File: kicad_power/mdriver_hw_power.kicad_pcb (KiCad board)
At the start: 4 copper layers, 115.4 x 107.7 mm, 69 parts, among them J1 Conn_02x05_Odd_Even, J2 Conn_01x02, M1 Fan, Q1 NMOS, Q2 NMOS, Q3 NMOS, Q4 NMOS, Q5 2N7002E, U7 SFH617A-1X007T

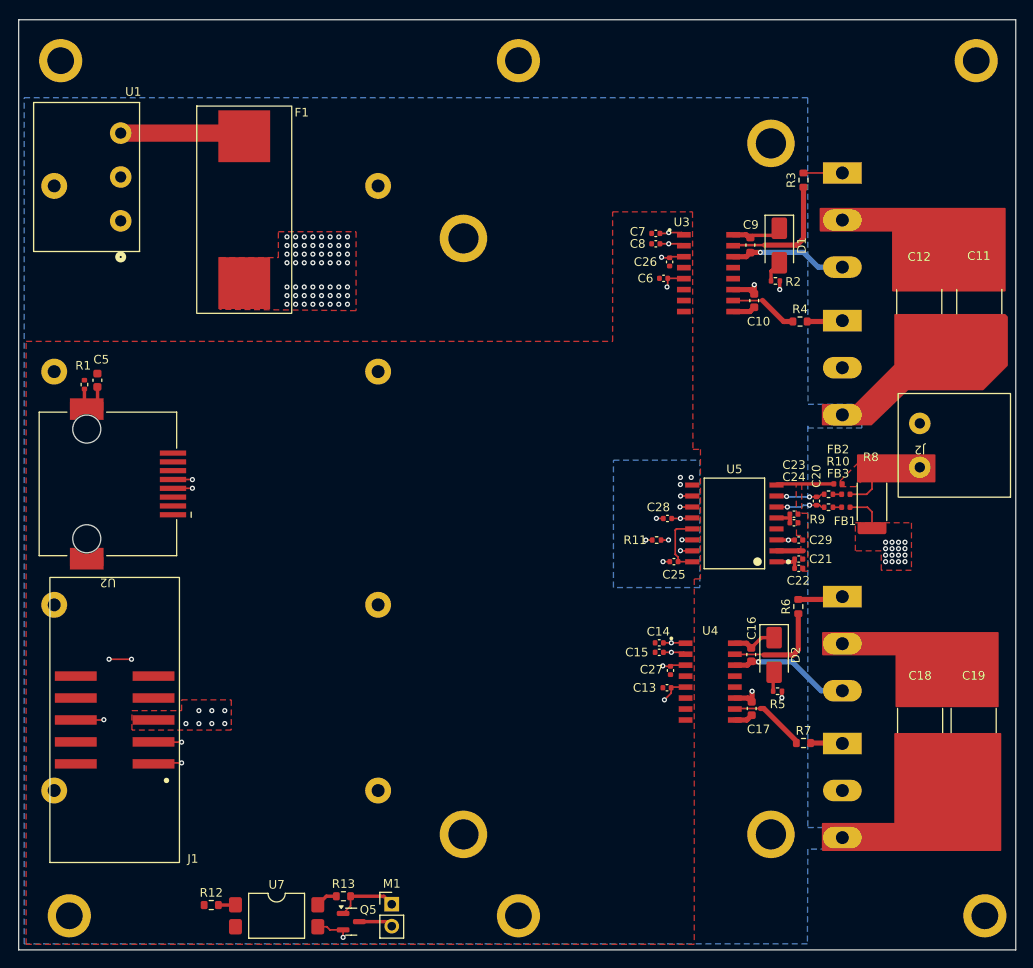
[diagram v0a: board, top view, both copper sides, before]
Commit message: adjustment to PCB layout, created BOM file, added MOSFET gate discharge diodes
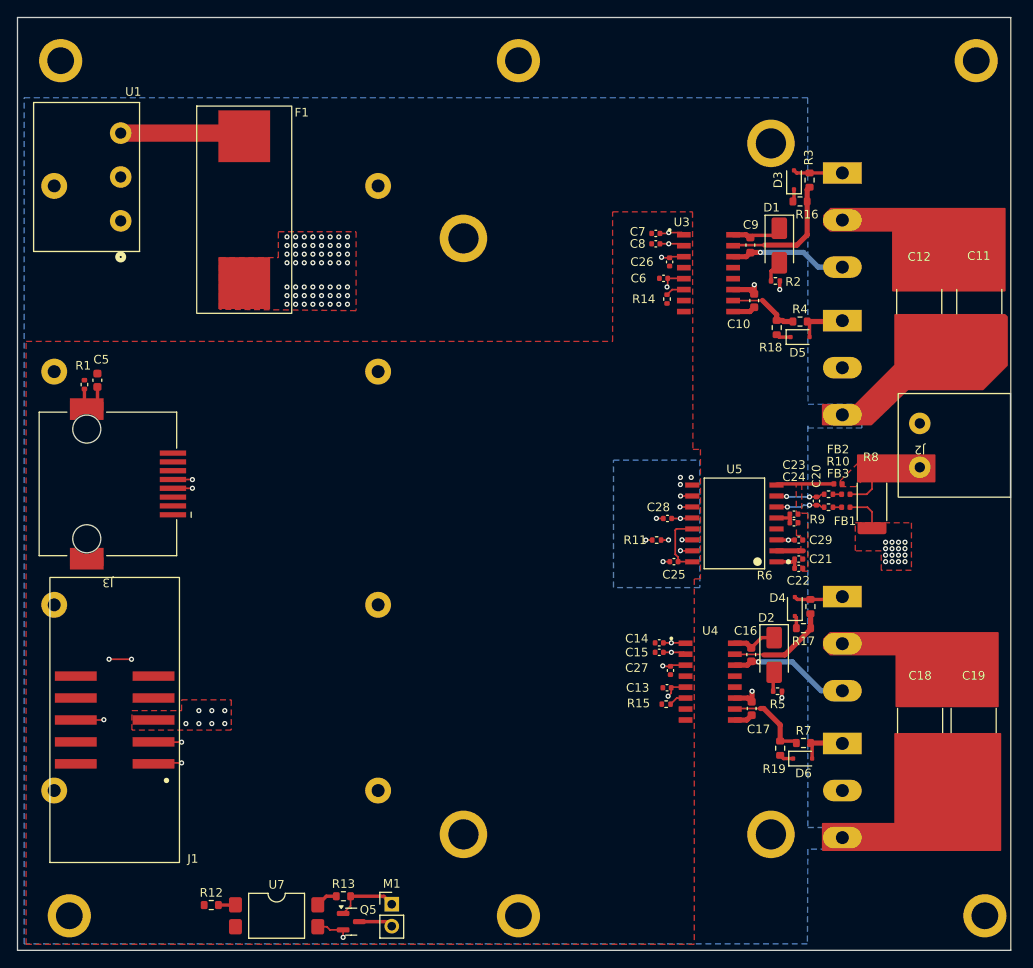
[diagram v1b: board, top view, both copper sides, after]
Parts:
- added D3: D_Schottky, Diode_SMD:D_SOD-323F, F.Cu at (153.9, 58.8)
- added D4: D_Schottky, Diode_SMD:D_SOD-323F, F.Cu at (154.0, 108.2)
- added D5: D_Schottky, Diode_SMD:D_SOD-323F, F.Cu at (154.6, 77.0)
- added D6: D_Schottky, Diode_SMD:D_SOD-323F, F.Cu at (154.9, 125.8)
- added R14: 0, Resistor_SMD:R_0402_1005Metric, F.Cu at (139.2, 72.6)
- added R15: 0, Resistor_SMD:R_0402_1005Metric, F.Cu at (139.1, 119.5)
- added R16: 3.3, Resistor_SMD:R_0603_1608Metric, F.Cu at (154.6, 61.3)
- added R17: 3.3, Resistor_SMD:R_0603_1608Metric, F.Cu at (155.0, 110.7)
- added R18: 3.3, Resistor_SMD:R_0603_1608Metric, F.Cu at (151.9, 75.9)
- added R19: 3.3, Resistor_SMD:R_0603_1608Metric, F.Cu at (152.3, 124.6)
- moved R6 1.40 mm to (155.8, 108.2)
- moved R3 0.70 mm to (155.7, 58.8)
- renumbered U2 to J3
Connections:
- U3 pad 6: ISOGND -> Net-(U3-DTC)
- U4 pad 6: ISOGND -> Net-(U4-DTC)
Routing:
- net Net-(U3-DTC): track 0.00 -> 2.19 mm
- net Net-(U4-DTC): track 0.00 -> 2.03 mm
- net Net-(D5-A): track 4.12 -> 6.03 mm
- net Net-(D6-A): track 3.70 -> 5.57 mm
- net Net-(D5-K): track 0.00 -> 1.71 mm
- net Net-(D6-K): track 0.00 -> 1.66 mm
- net Net-(D3-A): track 4.75 -> 6.26 mm
- net Net-(D4-K): track 0.00 -> 1.47 mm
- net Net-(D3-K): track 0.00 -> 1.45 mm
- net Net-(U4-OUTB): track 8.94 -> 10.1 mm
- net Net-(D4-A): track 5.23 -> 5.75 mm
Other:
- board size 115.4 x 107.7 mm -> 115 x 108 mm

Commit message: introduced AGND and A3V3, ensures HV design rules
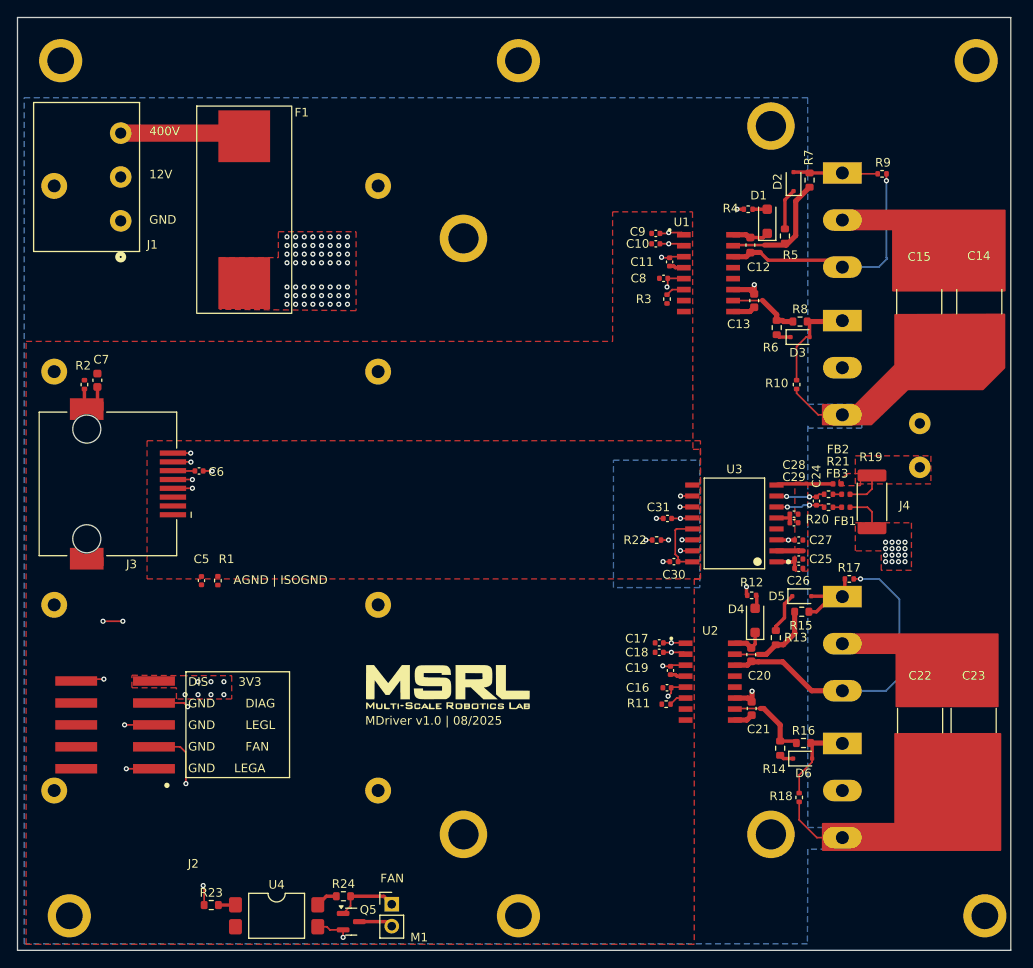
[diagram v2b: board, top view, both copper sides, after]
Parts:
- added C5: C, Capacitor_SMD:C_0402_1005Metric, F.Cu at (85.3, 105.2)
- added C6: 100nF, Capacitor_SMD:C_0402_1005Metric, F.Cu at (85.0, 92.5)
- added G***: LOGO, mdriver:msrl_logo, F.Cu at (114.2, 117.0)
- added R1: R, Resistor_SMD:R_0402_1005Metric, F.Cu at (87.2, 105.2)
- added R10: 560k, Resistor_SMD:R_0402_1005Metric, F.Cu at (154.2, 82.5)
- added R17: 560k, Resistor_SMD:R_0402_1005Metric, F.Cu at (160.3, 105.0)
- added R18: 560k, Resistor_SMD:R_0402_1005Metric, F.Cu at (154.5, 130.3)
- added R9: 560k, Resistor_SMD:R_0402_1005Metric, F.Cu at (164.1, 58.1)
- C12: renamed from C9; value 1uF -> 2.2u
- C13: renamed from C10; value 1uF -> 2.2u
- C20: renamed from C16; value 1uF -> 2.2u
- C21: renamed from C17; value 1uF -> 2.2u
- D1: footprint Diode_SMD:D_SMA -> Diode_SMD:D_SOD-123F
- D4: renamed from D2; footprint Diode_SMD:D_SMA -> Diode_SMD:D_SOD-123F
- R19: renamed from R8; value 3m -> 5m
- moved R12 11.5 mm to (149.0, 106.9), turned to 0 degrees
- moved R4 8.88 mm to (148.6, 62.2), turned to 0 degrees
- moved D4 4.57 mm to (149.4, 109.8), turned to 90 degrees
- moved R5 4.37 mm to (152.8, 65.3), turned to 90 degrees
- moved R13 3.38 mm to (151.8, 111.8), turned to 90 degrees
- moved D1 3.13 mm to (150.8, 63.6), turned to 90 degrees
- moved D5 1.44 mm to (154.8, 107.0), turned to 0 degrees
- moved R15 1.17 mm to (154.8, 108.8), turned to 0 degrees
- moved J2 0.57 mm to (75.3, 121.9)
- moved D2 0.21 mm to (153.8, 59.0)
- moved FB3 0.10 mm to (158.9, 94.0)
- renumbered C8 to C10, C26 to C11, C11 to C14, C12 to C15, C13 to C16, C14 to C17, C15 to C18, C27 to C19, C18 to C22, C19 to C23, C20 to C24, C21 to C25, C22 to C26, C29 to C27, C23 to C28, C24 to C29, C25 to C30, C28 to C31, C5 to C7, C6 to C8, C7 to C9, D3 to D2, D5 to D3, D4 to D5, U1 to J1, J1 to J2, J2 to J4, R15 to R11, R5 to R12, R17 to R13, R19 to R14, R6 to R15, R7 to R16, R1 to R2, R9 to R20, R10 to R21, R11 to R22, R12 to R23, R13 to R24, R14 to R3, R2 to R4, R16 to R5, R18 to R6, R3 to R7, R4 to R8, U3 to U1, U4 to U2, U5 to U3, U7 to U4
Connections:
- C30 pad 2: ISOGND -> AGND
- C31 pad 1: 3V3 -> A3V3
- C31 pad 2: ISOGND -> AGND
- J2 pad 2: ISOGND -> FAN
- J2 pad 4: ISOGND -> DIAG
- J3 pad 1: unconnected-(J3-Pad1) -> AGND
- J3 pad 2: unconnected-(J3-Pad2) -> AGND
- J3 pad 3: unconnected-(J3-Pad3) -> AGND
- J3 pad 6: unconnected-(J3-Pad6) -> /3V0ref
- J3 pad 7: unconnected-(J3-Pad7) -> A3V3
- J3 pad 8: unconnected-(J3-Pad8) -> A3V3
- R22 pad 1: 3V3 -> A3V3
- R22 pad 2: /isense/diag -> DIAG
- R23 pad 1: /fan/fan -> FAN
- U3 pad 12: 3V3 -> A3V3
- U3 pad 14: /isense/diag -> DIAG
- U3 pad 15: ISOGND -> AGND
- U3 pad 9: ISOGND -> AGND
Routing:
- net DIAG: track 0.00 -> 71.4 mm, vias 0 -> 3
- net /isense/in+: track 18.7 -> 41.3 mm
- net FAN: track 0.00 -> 22.5 mm, vias 0 -> 2
- net /legA/OUT: track 13.9 -> 29.4 mm
- net GND: track 3.95 -> 18.7 mm
- net A3V3: track 0.00 -> 7.31 mm, vias 0 -> 4
- net Net-(D5-A): track 5.75 -> 12.7 mm
- net DIS: track 200.1 -> 193.7 mm
- net Net-(D3-A): track 6.03 -> 11.9 mm
- net Net-(D6-A): track 5.57 -> 10.2 mm
- net LEGAH: track 194.4 -> 198.9 mm
- net Net-(D2-A): track 6.26 -> 10.4 mm
- net AGND: track 0.00 -> 3.76 mm, vias 0 -> 4
- net /isense/diag: track 3.66 -> 0.00 mm, vias 2 -> 0
- net Net-(D2-K): track 1.45 -> 4.79 mm
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- added copper zone on In1.Cu, net A3V3
- added copper zone on B.Cu, net AGND
- added copper zone on F.Cu, net AGND
- removed copper zone on B.Cu, net ISOGND
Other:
- board text added: "12V"
- board text added: "400V"
- board text added: "AGND | ISOGND"
- board text added: "DIS 3V3"
- board text added: "FAN"
- board text added: "GND"
- board text added: "GND DIAG"
- board text added: "GND FAN"
- board text added: "GND LEGA"
- board text added: "GND LEGL"
- board text added: "MDriver v1.0 | 08/2025"

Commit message: finished initial version of power PCB
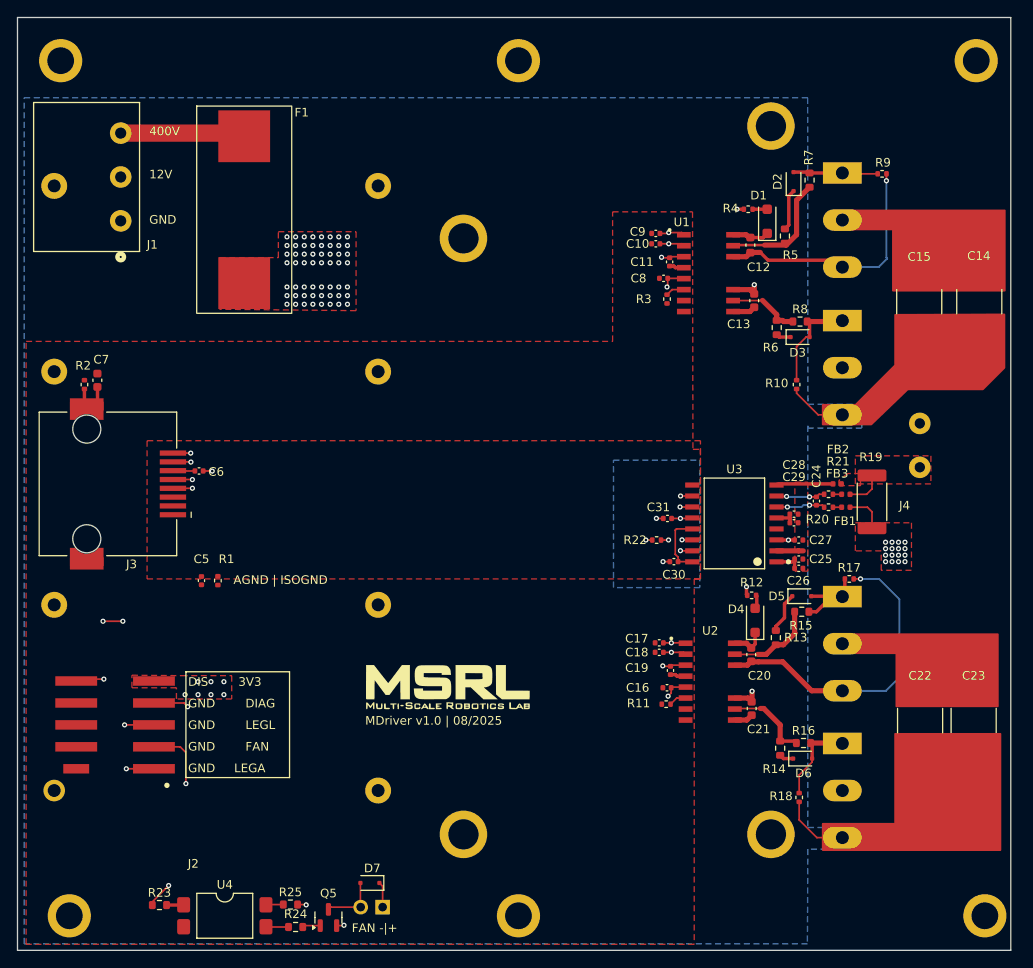
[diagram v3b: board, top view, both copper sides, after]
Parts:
- added D7: D_Schottky, Diode_SMD:D_SOD-323F, F.Cu at (104.8, 140.2)
- added R25: 430, Resistor_SMD:R_0603_1608Metric, F.Cu at (95.6, 142.7)
- M1: moved to B.Cu
- Q5: value 2N7002E -> BC817
- R24: value 2k -> 430
- moved R24 6.58 mm to (96.2, 145.3), turned to 180 degrees
- moved R23 6.00 mm to (80.4, 142.8)
- moved U4 6.00 mm to (88.0, 144.0)
- moved Q5 2.68 mm to (100.0, 144.2), turned to 90 degrees
- moved M1 1.11 mm to (106.3, 143.0), turned to 90 degrees
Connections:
- Q5 pad 1: 12V -> Net-(Q5-B)
- R24 pad 1: Net-(R24-Pad1) -> Net-(Q5-B)
- R24 pad 2: 12V -> Net-(R24-Pad2)
- U4 pad 3: GND -> Net-(R24-Pad2)
- U4 pad 4: Net-(R24-Pad1) -> Net-(R25-Pad1)
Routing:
- net 12V: track 16.4 -> 12.9 mm, vias 4 -> 5
- net GND: track 18.7 -> 15.6 mm
- net Net-(D7-A): track 3.97 -> 6.66 mm
- net Net-(R24-Pad2): track 0.00 -> 2.62 mm
- net Net-(R24-Pad1): track 2.56 -> 0.00 mm
- net Net-(Q5-B): track 0.00 -> 2.09 mm
- net Net-(R25-Pad1): track 0.00 -> 2.02 mm
- net FAN: track 22.5 -> 23.2 mm
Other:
- board text added: "FAN +|-"
- board text added: "FAN -|+"
- board text removed: "FAN"

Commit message: finished version 1.1 of power board
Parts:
- added C32: 100nF, Capacitor_SMD:C_0402_1005Metric, F.Cu at (139.1, 74.3)
- added C33: 100nF, Capacitor_SMD:C_0402_1005Metric, F.Cu at (138.9, 121.3)
- added C34: 2.2u, Capacitor_SMD:C_0603_1608Metric, F.Cu at (105.1, 140.6)
- added R26: 68k, Resistor_SMD:R_2512_6332Metric, F.Cu at (114.0, 53.1)
- added R27: 68k, Resistor_SMD:R_2512_6332Metric, F.Cu at (114.0, 57.3)
- C7: value 1uF -> 2.2u
- R12, R4: value 10 -> 18; footprint Resistor_SMD:R_0402_1005Metric -> Resistor_SMD:R_1206_3216Metric
- R13, R5: value 3.3 -> 0
- R15, R7: value 3.3 -> 12
- U1, U2: value ~ -> 2EDB8259Y
- U3: footprint mdriver:PAMC3302DWER -> mdriver:AMC3302DWER
- moved C6 3.00 mm to (85.1, 95.5)
- moved D7 1.65 mm to (105.1, 138.6)
- moved R4 1.30 mm to (147.3, 62.2)
- moved R12 1.29 mm to (147.9, 106.2)
- moved D4 0.05 mm to (149.3, 109.8)
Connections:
- C13 pad 2: Net-(U1-GNDB) -> GND
- C21 pad 2: Net-(U2-GNDB) -> GND
- J3 pad 1: AGND -> A3V3
- J3 pad 2: AGND -> A3V3
- J3 pad 3: AGND -> /3V0ref
- J3 pad 6: /3V0ref -> AGND
- J3 pad 7: A3V3 -> AGND
- J3 pad 8: A3V3 -> AGND
- U1 pad 8: ISOGND -> 3V3
- U1 pad 9: Net-(U1-GNDB) -> GND
- U2 pad 8: ISOGND -> 3V3
- U2 pad 9: Net-(U2-GNDB) -> GND
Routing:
- net 12V: track 12.9 -> 19.4 mm, vias 5 -> 8
- net 3V3: track 5.38 -> 10.4 mm, vias 9 -> 11
- net GND: track 15.6 -> 20.5 mm, vias 1 -> 5
- net Net-(U1-GNDB): track 2.65 -> 0.00 mm
- net Net-(U2-GNDB): track 2.18 -> 0.00 mm
- net Net-(D7-A): track 6.66 -> 8.70 mm
- net AGND: track 3.76 -> 2.75 mm, vias 4 -> 3
- net A3V3: track 7.31 -> 8.16 mm
- net Net-(D4-A): track 1.61 -> 2.21 mm
- added copper zone on F.Cu, net GND
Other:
- board text added: "MDriver v1.1 | 09/2025"
- board text removed: "MDriver v1.0 | 08/2025"
